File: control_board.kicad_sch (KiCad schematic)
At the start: 23 parts, among them IC6 ESP32-S3-WROOM-1-N8R8, J5 Conn_01x06_Pin, J6 USB_C_Receptacle_USB2.0_16P, SW2 SW, SW3 SW, U5 AMS1117-3.3

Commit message: add capacitors, move B pwr control, select remaining components
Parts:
- added R7, R9: 330R, Resistor_SMD:R_0402_1005Metric, symbol Device:R
- renumbered C2 to C10, C3 to C11, C4 to C12, C5 to C13, C6 to C14, C1 to C9, IC6 to IC7, J6 to J4, R6 to R10, R7 to R11, R8 to R12, R9 to R5, R10 to R6, R5 to R8, SW2 to SW1, SW3 to SW2
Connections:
- net at C11.1, R8.2, SW1.2: now also R7.2; no longer IC7.11 (IO18)
- net at C14.1, R10.2, SW2.2: now also R9.2; no longer IC7.12 (IO8)
- new net: IC7.11 (IO18), R7.1
- new net: IC7.12 (IO8), R9.1
- no-connect marks 28 -> 27

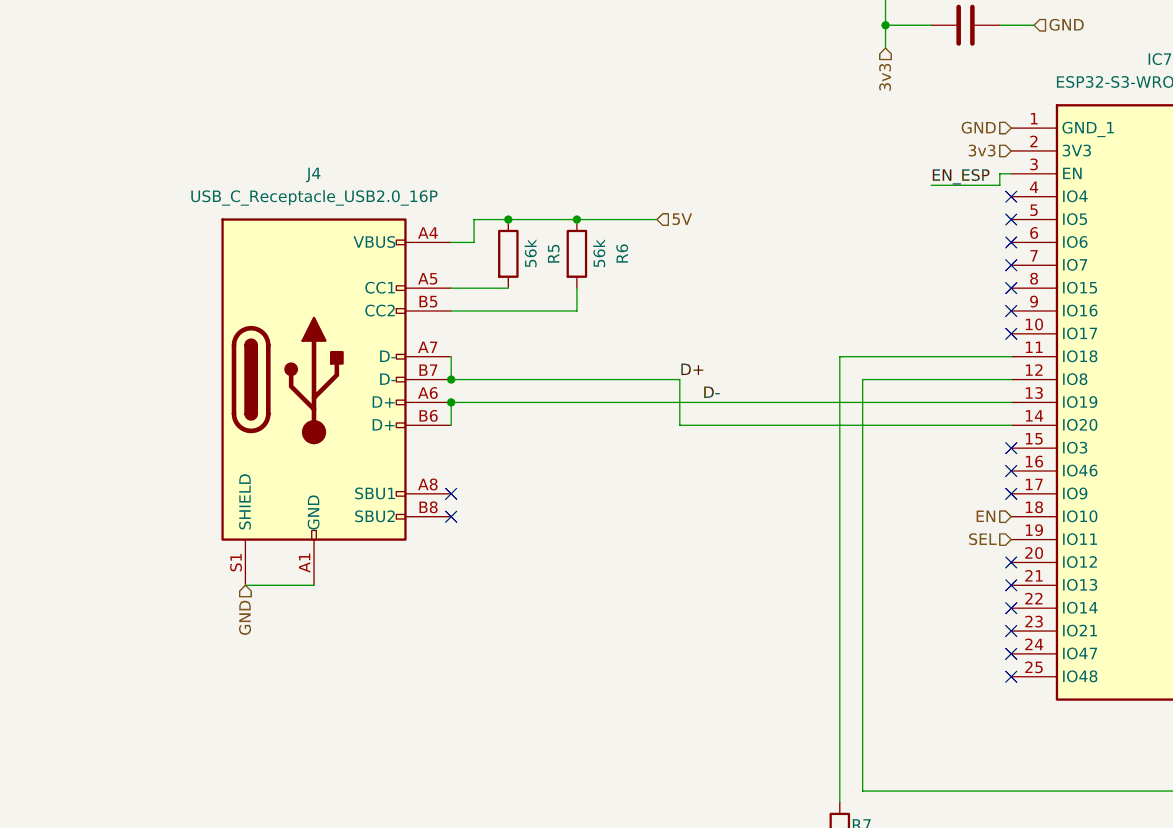
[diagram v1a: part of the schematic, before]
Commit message: fix usb connections, board dimensions
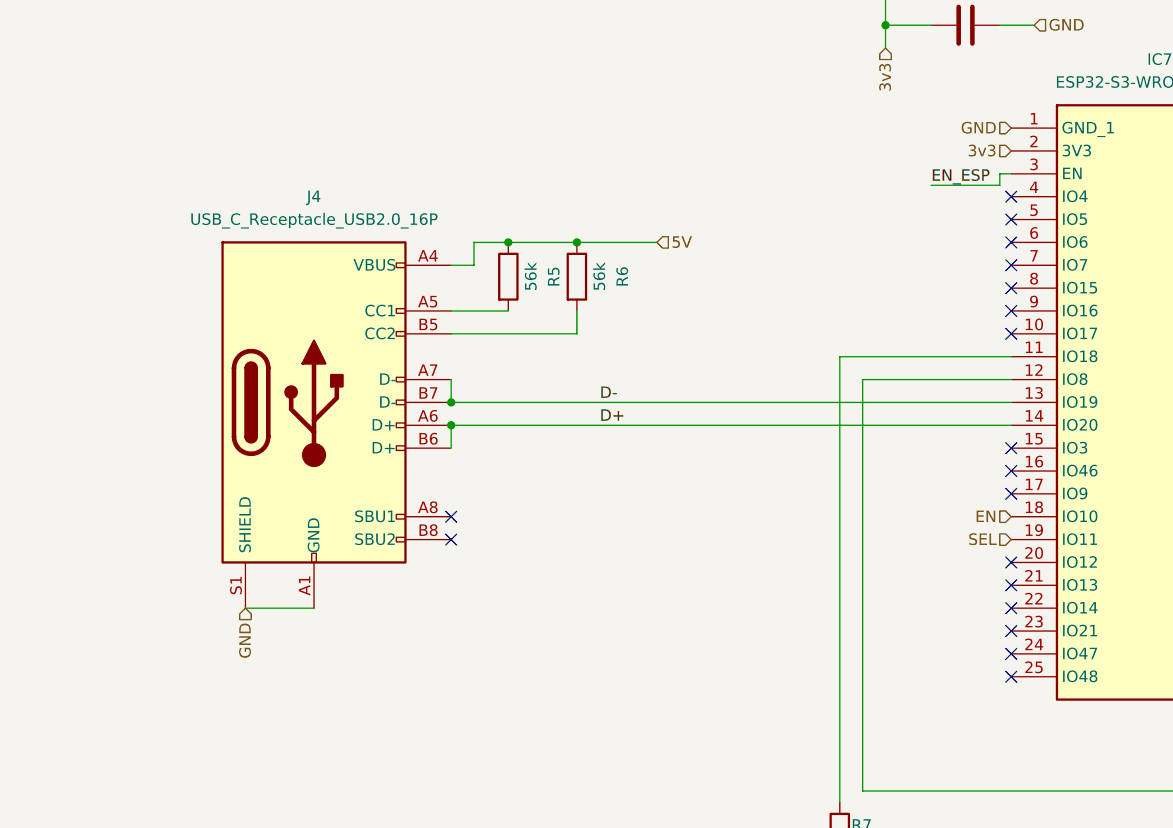
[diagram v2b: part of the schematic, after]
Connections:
- net D+: now also J4.A6 (D+), J4.B6 (D+); no longer J4.A7 (D-), J4.B7 (D-)
- net D-: now also J4.A7 (D-), J4.B7 (D-); no longer J4.A6 (D+), J4.B6 (D+)
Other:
- moved on the sheet: J4, R5, R6

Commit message: fixes
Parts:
- added R13, R14: 330R, Resistor_SMD:R_0402_1005Metric, symbol Device:R
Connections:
- net EN: now also R13.1; no longer IC7.18 (IO10)
- net SEL: now also R14.1; no longer IC7.19 (IO11)
- new net: IC7.18 (IO10), R13.2
- new net: IC7.19 (IO11), R14.2
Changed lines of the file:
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@@
+	(wire
+		(pts
+			(xy 91.44 93.98) (xy 91.44 91.44)
+		)
+		(stroke
+			(width 0)
+			(type default)
+		)
+	)
 	(wire
 		(pts
@@
 	(wire
 		(pts
+			(xy 100.33 101.6) (xy 100.33 105.41)
+		)
+		(stroke
+			(width 0)
+			(type default)
+		)
+	)
+	(wire
+		(pts
 			(xy 69.85 76.2) (xy 69.85 78.74)
 		)
@@
 	(wire
 		(pts
+			(xy 91.44 91.44) (xy 132.08 91.44)
+		)
+		(stroke
+			(width 0)
+			(type default)
+		)
+	)
+	(wire
+		(pts
 			(xy 130.81 54.61) (xy 123.19 54.61)
 		)
@@
 	(wire
 		(pts
+			(xy 100.33 93.98) (xy 132.08 93.98)
+		)
+		(stroke
+			(width 0)
+			(type default)
+		)
+	)
+	(wire
+		(pts
 			(xy 152.4 121.92) (xy 152.4 123.19)
 		)
@@
 		(pts
 			(xy 69.85 81.28) (xy 132.08 81.28)
+		)
+		(stroke
+			(width 0)
+			(type default)
+		)
+	)
+	(wire
+		(pts
+			(xy 91.44 105.41) (xy 91.44 101.6)
 		)
 		(stroke
@@
 	(hierarchical_label "EN"
 		(shape input)
-		(at 132.08 91.44 180)
+		(at 91.44 105.41 270)
 		(fields_autoplaced yes)
 		(effects
@@
 	(hierarchical_label "SEL"
 		(shape input)
-		(at 132.08 93.98 180)
+		(at 100.33 105.41 270)
 		(fields_autoplaced yes)
 		(effects
@@
 				(path "/79003e62-8193-4467-8c13-bb2f1c773c85/75ff4b9f-aa1b-49d1-a6d7-3531ac2b67a9"
 					(reference "C13")
+					(unit 1)
+				)
+			)
+		)
+	)
+	(symbol
+		(lib_id "Device:R")
+		(at 100.33 97.79 180)
+		(unit 1)
+		(exclude_from_sim no)
+		(in_bom yes)
+		(on_board yes)
+		(dnp no)
+		(property "Reference" "R14"
+			(at 99.06 99.06 0)
+			(effects
+				(font
+					(size 1.27 1.27)
+				)
+				(justify left)
+			)
+		)
+		(property "Value" "330R"
+			(at 99.06 96.52 0)
+			(effects
+				(font
+					(size 1.27 1.27)
+				)
+				(justify left)
+			)
+		)
+		(property "Footprint" "Resistor_SMD:R_0402_1005Metric"
+			(at 102.108 97.79 90)
+			(effects
+				(font
+					(size 1.27 1.27)
+				)
+				(hide yes)
+			)
+		)
+		(property "Datasheet" "~"
+			(at 100.33 97.79 0)
+			(effects
+				(font
+					(size 1.27 1.27)
+				)
+				(hide yes)
+			)
+		)
+		(property "Description" ""
+			(at 100.33 97.79 0)
+			(effects
+				(font
+					(size 1.27 1.27)
+				)
+				(hide yes)
+			)
+		)
+		(property "LCSC" "C25744"
+			(at 100.33 97.79 0)
+			(effects
+				(font
+					(size 1.27 1.27)
+				)
+				(hide yes)
+			)
+		)
+		(property "JLCPCB_CORRECTION" ""
+			(at 100.33 97.79 0)
+			(effects
+				(font
+					(size 1.27 1.27)
+				)
+				(hide yes)
+			)
+		)
+		(property "Basic/Extended" "B"
+			(at 100.33 97.79 0)
+			(effects
+				(font
+					(size 1.27 1.27)
+				)
+				(hide yes)
+			)
+		)
+		(pin "1"
+		)
+		(pin "2"
+		)
+		(instances
+			(project "usb-switch"
+				(path "/79003e62-8193-4467-8c13-bb2f1c773c85/75ff4b9f-aa1b-49d1-a6d7-3531ac2b67a9"
+					(reference "R14")
 					(unit 1)
 				)
@@
 					(unit 1)
 				)
+			)
+		)
+	)
+	(symbol
+		(lib_id "Device:R")
+		(at 91.44 97.79 180)
+		(unit 1)
+		(exclude_from_sim no)
+		(in_bom yes)
+		(on_board yes)
+		(dnp no)
+		(property "Reference" "R13"
+			(at 90.17 99.06 0)
+			(effects
+				(font
+					(size 1.27 1.27)
+				)
+				(justify left)
+			)
+		)
+		(property "Value" "330R"
+			(at 90.17 96.52 0)
+			(effects
+				(font
+					(size 1.27 1.27)
+				)
+				(justify left)
+			)
+		)
+		(property "Footprint" "Resistor_SMD:R_0402_1005Metric"
+			(at 93.218 97.79 90)
+			(effects
+				(font
+					(size 1.27 1.27)
+				)
+				(hide yes)
+			)
+		)
+		(property "Datasheet" "~"
+			(at 91.44 97.79 0)
+			(effects
+				(font
+					(size 1.27 1.27)
+				)
+				(hide yes)
+			)
+		)
+		(property "Description" ""
+			(at 91.44 97.79 0)
+			(effects
+				(font
+					(size 1.27 1.27)
+				)
+				(hide yes)
+			)
+		)
+		(property "LCSC" "C25744"
+			(at 91.44 97.79 0)
+			(effects
+				(font
+					(size 1.27 1.27)
+				)
+				(hide yes)
+			)
+		)
+		(property "JLCPCB_CORRECTION" ""
+			(at 91.44 97.79 0)
+			(effects
+				(font
+					(size 1.27 1.27)
+				)
+				(hide yes)
+			)
+		)
+		(property "Basic/Extended" "B"
+			(at 91.44 97.79 0)
+			(effects
+				(font
+					(size 1.27 1.27)
+				)
+				(hide yes)
+			)
+		)
+		(pin "1"
+		)
+		(pin "2"
+		)
+		(instances
+			(project "usb-switch"
+				(path "/79003e62-8193-4467-8c13-bb2f1c773c85/75ff4b9f-aa1b-49d1-a6d7-3531ac2b67a9"
+					(reference "R13")
+					(unit 1)
+				)
